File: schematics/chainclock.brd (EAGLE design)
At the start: 72.7 x 40 mm, 19 parts, among them SW1 ROTARTY_ENCODER

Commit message: Update layout
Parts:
- removed R11, R12, R5, R6: 10k, SparkFun-Resistors:R2010
- added R1, R2, R7, R8: 10k, SparkFun-Resistors:AXIAL-0.3EZ
- moved C6 47.8 mm to (25.4, 36.2)
- moved C5 45.5 mm to (22.9, 36.2), turned to 90 degrees
- moved R4 14.7 mm to (45.7, 28.6)
- moved U$4 7.65 mm to (33.7, 29.2)
- moved C4 0.64 mm to (37.5, 36.2)
- moved PTN0405 0.64 mm to (47.0, 38.8)
- moved ARDUNOFIO 0.63 mm to (39.4, 6.99)
- moved C3 0.63 mm to (30.6, 36.2)
- moved HBRIDGE 0.63 mm to (34.7, 15.6)
- moved R3 0.63 mm to (40.6, 26.0)
- moved STEPPER 0.63 mm to (43.2, 29.8)
- moved SW1 0.63 mm to (52.7, 9.53)
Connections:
- net 3V32: now also R1.P$2, R2.P$2; no longer R11.2, R12.2
- net N$2: now also R1.P$1, R7.P$2; no longer R11.1, R5.1
- net N$5: now also R2.P$1, R8.P$2; no longer R12.1, R6.2
- net RENCA: now also ARDUNOFIO.21, R8.P$1; no longer ARDUNOFIO.13, R6.1
- net RENCB: now also ARDUNOFIO.20, R7.P$1; no longer ARDUNOFIO.12, R5.2
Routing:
- net N$5: track 15.8 -> 59.3 mm
- net N$2: track 16.1 -> 58.4 mm
- net 3V32: track 98.5 -> 59.3 mm
- net RENCA: track 39.1 -> 6.75 mm
- net RENCB: track 42.2 -> 11.6 mm
- net GND: track 9.65 -> 0.00 mm
- net N$3: track 14.6 -> 7.74 mm
- net RTC: track 3.38 -> 8.66 mm
- net RENBTN: track 28.6 -> 26.5 mm
- net VDD12: track 43.6 -> 42.2 mm
- net 2Y: track 18.1 -> 18.7 mm
- added copper zone on layer 1, net GND

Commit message: New board layout
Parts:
- moved U$2 25.8 mm to (81.8, 19.9)
- moved SW1 2.00 mm to (54.7, 9.53)
- moved U$3 1.00 mm to (66.9, 29.8)
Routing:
- net N$5: track 59.3 -> 61.4 mm
- net N$2: track 58.4 -> 60.4 mm
- net RENBTN: track 26.5 -> 28.5 mm
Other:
- board size 72.7 x 40 mm -> 72 x 39.5 mm
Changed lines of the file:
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@@
 <setting verticaltext="up"/>
 </settings>
-<grid distance="0.025" unitdist="inch" unit="inch" style="lines" multiple="1" display="yes" altdistance="0.025" altunitdist="inch" altunit="inch"/>
+<grid distance="0.5" unitdist="mm" unit="mm" style="lines" multiple="1" display="yes" altdistance="0.025" altunitdist="inch" altunit="inch"/>
 <layers>
 <layer number="1" name="Top" color="4" fill="1" visible="yes" active="yes"/>
@@
 <board>
 <plain>
-<hole x="3.175" y="3.175" drill="2.8"/>
-<hole x="3.175" y="36.83" drill="2.8"/>
-<wire x1="0" y1="0" x2="0" y2="40" width="0.254" layer="20"/>
-<wire x1="0" y1="40" x2="72.7" y2="40" width="0.254" layer="20"/>
-<wire x1="72.7" y1="0" x2="0" y2="0" width="0.254" layer="20"/>
-<hole x="62.23" y="19.685" drill="2.8"/>
-<wire x1="72.7" y1="0" x2="72.7" y2="12" width="0.254" layer="20"/>
-<wire x1="72.7" y1="12" x2="69.7" y2="15" width="0.254" layer="20" curve="-90"/>
-<wire x1="69.7" y1="15" x2="69.7" y2="24" width="0.254" layer="20"/>
-<wire x1="69.7" y1="24" x2="72.7" y2="27" width="0.254" layer="20" curve="-90"/>
-<wire x1="72.7" y1="27" x2="72.7" y2="40" width="0.254" layer="20"/>
+<hole x="3" y="3" drill="2.8"/>
+<hole x="3" y="37" drill="2.8"/>
+<hole x="62" y="20" drill="2.8"/>
 <text x="6.985" y="34.29" size="1.016" layer="21">v1.0 (c) 2014
 cjd@chrisd.info
 http://blog.chrisd.info</text>
-<hole x="43.18" y="3.175" drill="2.8"/>
-<hole x="43.18" y="36.83" drill="2.8"/>
+<hole x="43" y="3" drill="2.8"/>
+<hole x="43" y="37" drill="2.8"/>
+<wire x1="0" y1="0" x2="0" y2="39.5" width="0.3048" layer="20"/>
+<wire x1="0" y1="39.5" x2="72" y2="39.5" width="0.3048" layer="20"/>
+<wire x1="72" y1="39.5" x2="72" y2="27" width="0.3048" layer="20"/>
+<wire x1="72" y1="27" x2="72" y2="12.5" width="0.3048" layer="20" curve="90"/>
+<wire x1="72" y1="12.5" x2="72" y2="0" width="0.3048" layer="20"/>
+<wire x1="0" y1="0" x2="72" y2="0" width="0.3048" layer="20"/>
 </plain>
 <attributes>
@@
 <element name="C4" library="SparkFun-Passives" package="CPOL-RADIAL-100UF-25V" value="" x="37.465" y="36.195" rot="R270"/>
 <element name="R4" library="SparkFun-Resistors" package="AXIAL-0.3EZ" value="1.35k" x="45.72" y="28.575" rot="R90"/>
-<element name="U$2" library="desjardins" package="NEMA14" value="" x="100.33" y="1.905" rot="R90"/>
-<element name="U$3" library="desjardins" package="LOGO" value="" x="67.945" y="29.845" rot="MR270"/>
-<element name="SW1" library="SparkFun-Electromechanical" package="ROTARY_ENC_PLAIN" value="ROTARTY_ENCODER" x="52.705" y="9.525" rot="MR180"/>
+<element name="U$2" library="desjardins" package="NEMA14" value="" x="81.83" y="19.905" rot="R90"/>
+<element name="U$3" library="desjardins" package="LOGO" value="" x="66.945" y="29.845" rot="MR270"/>
+<element name="SW1" library="SparkFun-Electromechanical" package="ROTARY_ENC_PLAIN" value="ROTARTY_ENCODER" x="54.705" y="9.525" rot="MR180"/>
 <element name="C5" library="SparkFun-Capacitors" package="CAP-PTH-SMALL-KIT" value=".01uf" x="22.86" y="36.195" rot="R90"/>
 <element name="C6" library="SparkFun-Capacitors" package="CAP-PTH-SMALL-KIT" value=".01uf" x="25.4" y="36.195" rot="R90"/>
@@
 <polygon width="0.4064" layer="16">
 <vertex x="1" y="1"/>
-<vertex x="1" y="39"/>
-<vertex x="72" y="39"/>
-<vertex x="72" y="28" curve="90"/>
-<vertex x="69" y="25"/>
-<vertex x="69" y="24"/>
-<vertex x="69" y="15"/>
-<vertex x="69" y="14" curve="90"/>
-<vertex x="72" y="11"/>
-<vertex x="72" y="1"/>
+<vertex x="1" y="38.5"/>
+<vertex x="71.5" y="38.5"/>
+<vertex x="71.5" y="28.5" curve="90"/>
+<vertex x="71.5" y="11"/>
+<vertex x="71.5" y="1"/>
 </polygon>
 <polygon width="0.4064" layer="1">
 <vertex x="1" y="1"/>
-<vertex x="1" y="39"/>
-<vertex x="72" y="39"/>
-<vertex x="72" y="28" curve="90"/>
-<vertex x="69" y="25"/>
-<vertex x="69" y="24"/>
-<vertex x="69" y="15"/>
-<vertex x="69" y="14" curve="90"/>
-<vertex x="72" y="11"/>
-<vertex x="72" y="1"/>
+<vertex x="1" y="38.5"/>
+<vertex x="71.5" y="38.5"/>
+<vertex x="71.5" y="28.5" curve="90"/>
+<vertex x="71.5" y="11"/>
+<vertex x="71.5" y="1"/>
 </polygon>
 </signal>
@@
 <wire x1="10.16" y1="31.115" x2="12.065" y2="33.02" width="0.4064" layer="16"/>
 <wire x1="12.065" y1="33.02" x2="28.655" y2="33.02" width="0.4064" layer="16"/>
-<wire x1="51.704" y1="37.236" x2="47.396" y2="37.236" width="0.4064" layer="16"/>
-<wire x1="47.396" y1="37.236" x2="43.815" y2="33.02" width="0.4064" layer="16"/>
 <wire x1="28.655" y1="33.02" x2="30.56" y2="34.925" width="0.4064" layer="16"/>
-<wire x1="43.815" y1="33.02" x2="32.465" y2="33.02" width="0.4064" layer="16"/>
+<wire x1="44.02" y1="33.02" x2="32.465" y2="33.02" width="0.4064" layer="16"/>
 <wire x1="32.465" y1="33.02" x2="30.56" y2="34.925" width="0.4064" layer="16"/>
+<wire x1="44.02" y1="33.02" x2="45" y2="34" width="0.4064" layer="16"/>
+<wire x1="45" y1="34" x2="48.468" y2="34" width="0.4064" layer="16"/>
+<wire x1="48.468" y1="34" x2="51.704" y2="37.236" width="0.4064" layer="16"/>
 </signal>
 <signal name="3V32">
@@
 <wire x1="15.875" y1="22.86" x2="21.59" y2="22.86" width="0.4064" layer="16"/>
 <wire x1="22.86" y1="17.78" x2="24.765" y2="15.875" width="0.4064" layer="16"/>
-<wire x1="24.765" y1="15.875" x2="44.45" y2="15.875" width="0.4064" layer="16"/>
-<wire x1="44.45" y1="15.875" x2="53.34" y2="6.985" width="0.4064" layer="16"/>
-<wire x1="53.34" y1="6.985" x2="60.198" y2="6.985" width="0.4064" layer="16"/>
+<wire x1="24.765" y1="15.875" x2="46.11" y2="15.875" width="0.4064" layer="16"/>
+<wire x1="55" y1="6.985" x2="62.198" y2="6.985" width="0.4064" layer="16"/>
 <wire x1="22.86" y1="17.78" x2="22.86" y2="21.59" width="0.4064" layer="16"/>
 <wire x1="22.86" y1="21.59" x2="21.59" y2="22.86" width="0.4064" layer="16"/>
+<wire x1="46.11" y1="15.875" x2="55" y2="6.985" width="0.4064" layer="16"/>
 </signal>
 <signal name="N$5">
@@
 <wire x1="24.13" y1="24.765" x2="24.13" y2="18.415" width="0.4064" layer="16"/>
 <wire x1="24.13" y1="18.415" x2="25.4" y2="17.145" width="0.4064" layer="16"/>
-<wire x1="25.4" y1="17.145" x2="45.72" y2="17.145" width="0.4064" layer="16"/>
-<wire x1="45.72" y1="17.145" x2="50.8" y2="12.065" width="0.4064" layer="16"/>
-<wire x1="50.8" y1="12.065" x2="60.198" y2="12.065" width="0.4064" layer="16"/>
+<wire x1="25.4" y1="17.145" x2="46.855" y2="17.145" width="0.4064" layer="16"/>
+<wire x1="46.855" y1="17.145" x2="52" y2="12" width="0.4064" layer="16"/>
+<wire x1="52" y1="12" x2="62.133" y2="12" width="0.4064" layer="16"/>
+<wire x1="62.133" y1="12" x2="62.198" y2="12.065" width="0.4064" layer="16"/>
 </signal>
 <signal name="RENBTN">
 <contactref element="SW1" pad="SW+"/>
 <contactref element="ARDUNOFIO" pad="7"/>
-<wire x1="45.085" y1="6.35" x2="22.225" y2="6.35" width="0.4064" layer="1"/>
+<wire x1="47.085" y1="6.35" x2="22.225" y2="6.35" width="0.4064" layer="1"/>
 <wire x1="22.225" y1="6.35" x2="20.32" y2="8.255" width="0.4064" layer="1"/>
-<wire x1="45.085" y1="6.35" x2="45.72" y2="6.985" width="0.4064" layer="1"/>
+<wire x1="47.085" y1="6.35" x2="47.72" y2="6.985" width="0.4064" layer="1"/>
 </signal>
 <signal name="RENCB">

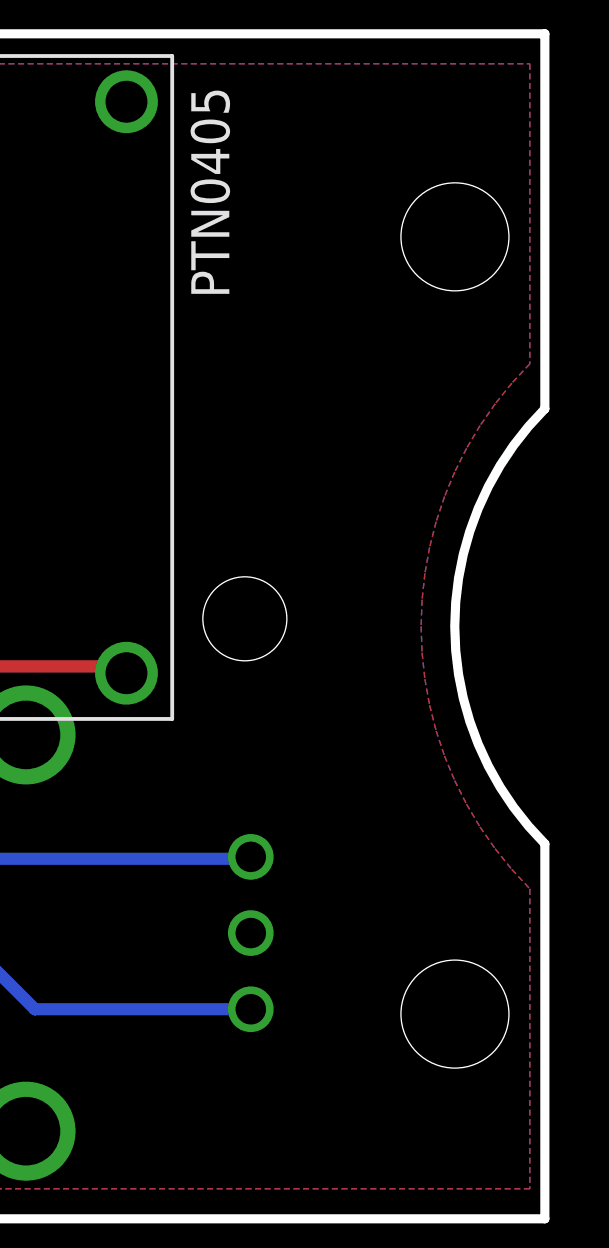
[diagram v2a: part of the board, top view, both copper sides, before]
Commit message: Center motor
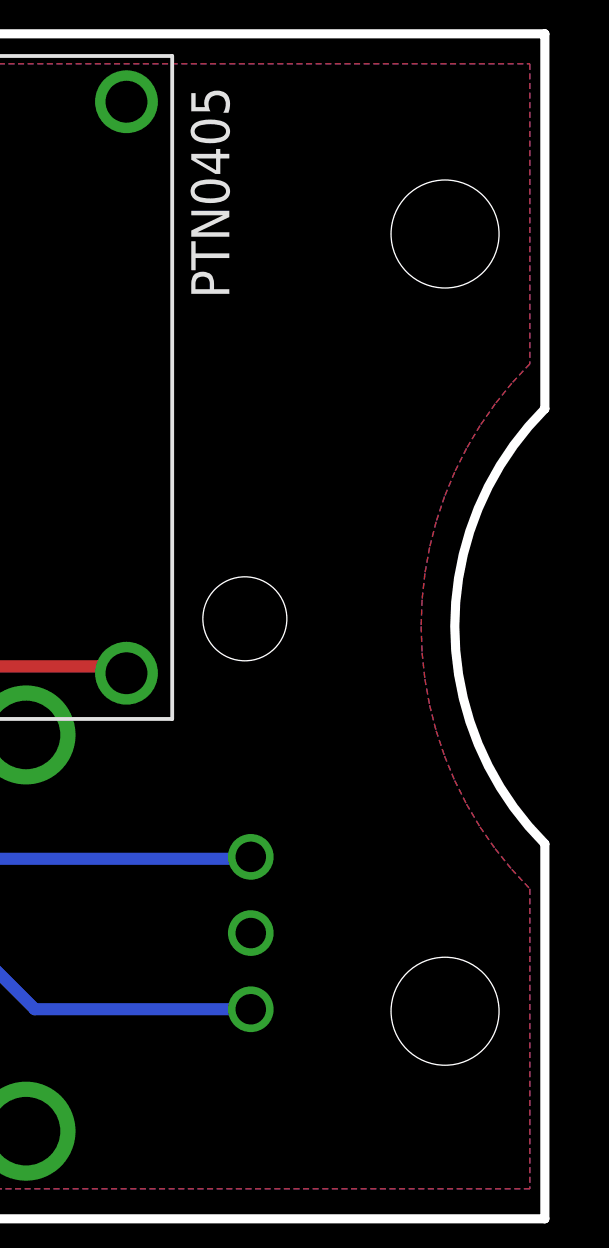
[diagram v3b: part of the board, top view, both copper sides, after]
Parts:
- moved U$2 0.34 mm to (81.5, 20.0)
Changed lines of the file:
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@@
 <element name="C4" library="SparkFun-Passives" package="CPOL-RADIAL-100UF-25V" value="" x="37.465" y="36.195" rot="R270"/>
 <element name="R4" library="SparkFun-Resistors" package="AXIAL-0.3EZ" value="1.35k" x="45.72" y="28.575" rot="R90"/>
-<element name="U$2" library="desjardins" package="NEMA14" value="" x="81.83" y="19.905" rot="R90"/>
+<element name="U$2" library="desjardins" package="NEMA14" value="" x="81.5" y="20" rot="R90"/>
 <element name="U$3" library="desjardins" package="LOGO" value="" x="66.945" y="29.845" rot="MR270"/>
 <element name="SW1" library="SparkFun-Electromechanical" package="ROTARY_ENC_PLAIN" value="ROTARTY_ENCODER" x="54.705" y="9.525" rot="MR180"/>
